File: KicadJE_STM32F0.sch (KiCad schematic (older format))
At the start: 65 parts

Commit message: USB - Boot sel - Serial - STM32
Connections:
- wire segments 136 -> 133
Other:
- moved on the sheet: C?, JP?, R?, SW?, U?, U?B

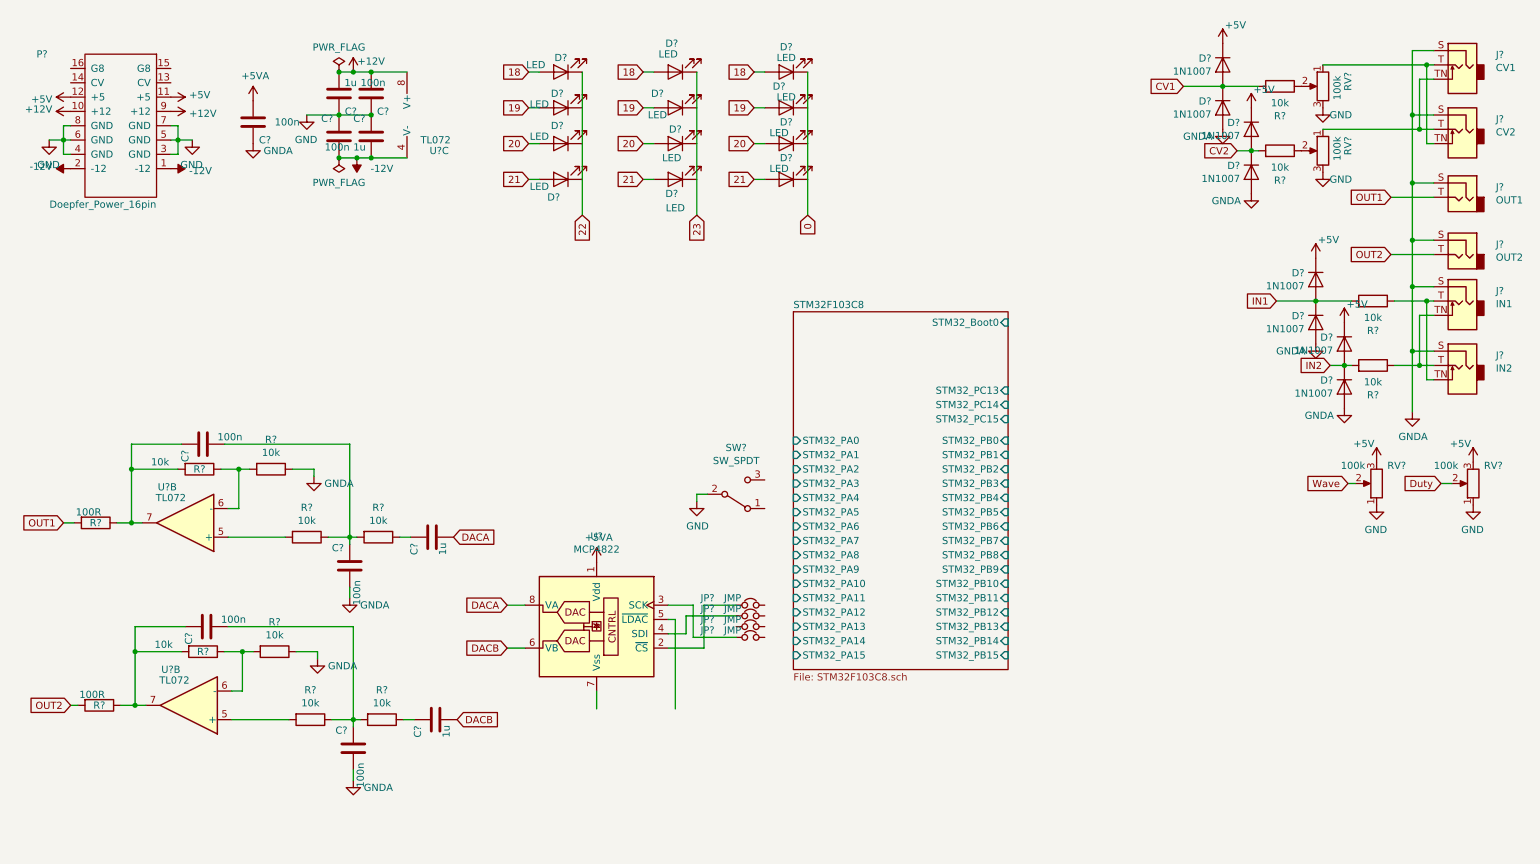
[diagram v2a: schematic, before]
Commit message: STM32 DAC and Analog input
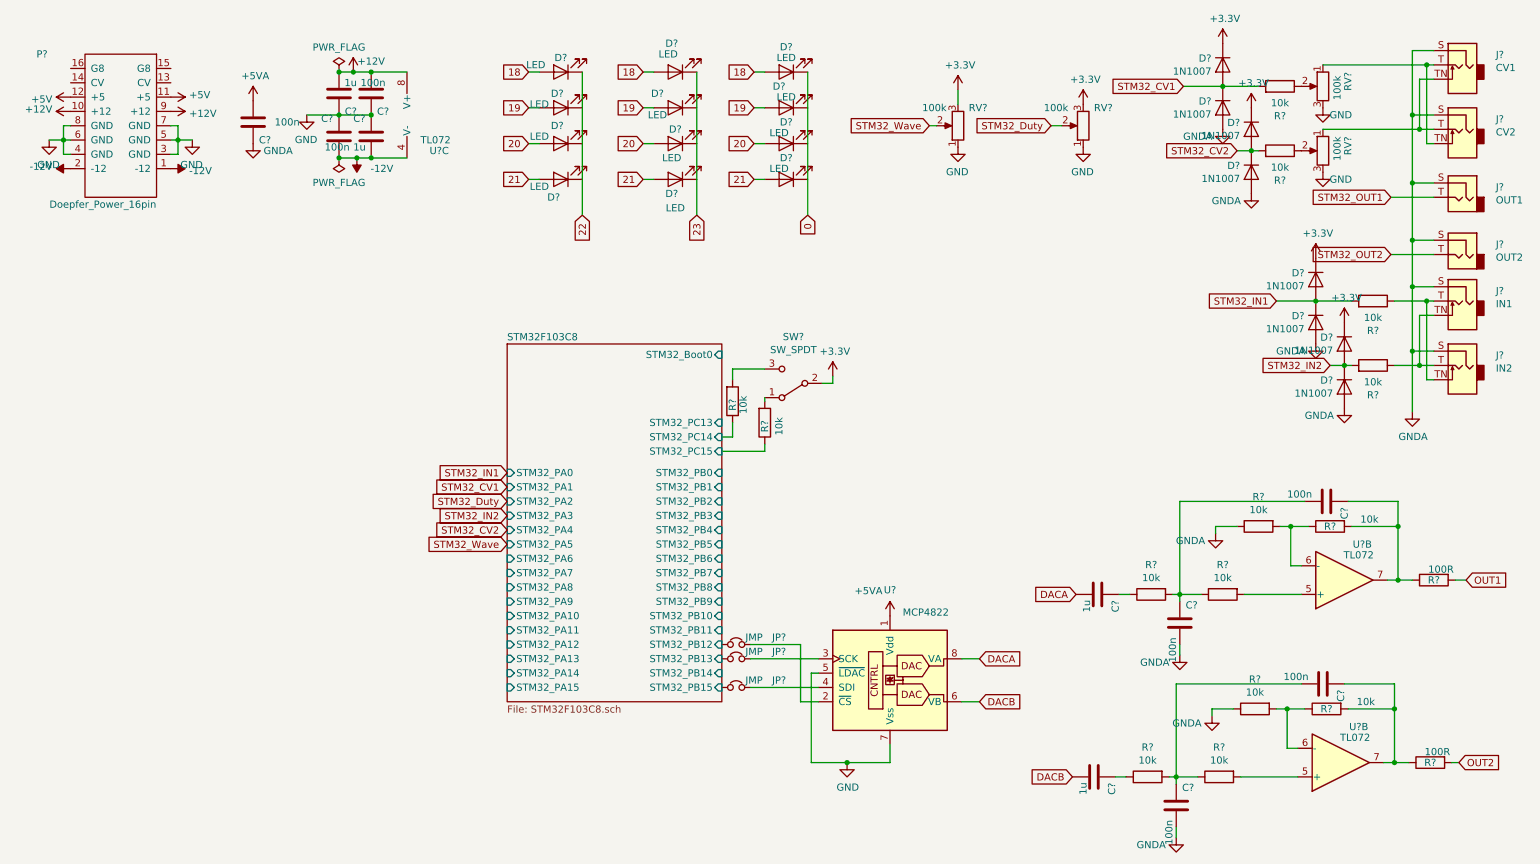
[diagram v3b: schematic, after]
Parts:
- removed JP?: JMP, Connector_PinSocket_2.54mm:PinSocket_1x02_P2.54mm_Vertical, symbol Device:Jumper_NC_Small
- added R? (x2): 10k, Resistor_SMD:R_0805_2012Metric_Pad1.15x1.40mm_HandSolder, symbol Device:R
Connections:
- net +5V: no longer D?.1 (K), D?.1 (K), D?.1 (K), D?.1 (K), RV?.3, RV?.3
- net GND: now also U?.5 (~LDAC), U?.7 (Vss); no longer SW?.2 (B)
- net OUT1: no longer J?.T
- net OUT2: no longer J?.T
- net STM32F103C8/STM32_PB12: now also JP?.2
- net STM32F103C8/STM32_PB13: now also JP?.2
- net STM32F103C8/STM32_PB15: now also JP?.2
- net STM32F103C8/STM32_PC14: now also R?.1
- net STM32F103C8/STM32_PC15: now also R?.1
- net at U?.3 (SCK): now also JP?.1
- net at U?.4 (SDI): now also JP?.1; no longer JP?.1
- net at SW?.1 (A): now also R?.2
- net at SW?.3 (C): now also R?.2
- net CV1 renamed STM32_CV1
- net CV2 renamed STM32_CV2
- net Duty renamed STM32_Duty
- net IN1 renamed STM32_IN1
- net IN2 renamed STM32_IN2
- net Wave renamed STM32_Wave
- new net +3V3: D?.1 (K), D?.1 (K), D?.1 (K), D?.1 (K), RV?.3, RV?.3, SW?.2 (B)
- new net STM32_OUT1: J?.T
- new net STM32_OUT2: J?.T
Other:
- moved on the sheet: C?, JP?, R?, RV?, SW?, U?, U?B
